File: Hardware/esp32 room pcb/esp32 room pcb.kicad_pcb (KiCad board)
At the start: 2 copper layers, 34.5 x 65.5 mm, 6 parts, among them Q1 AO3400A

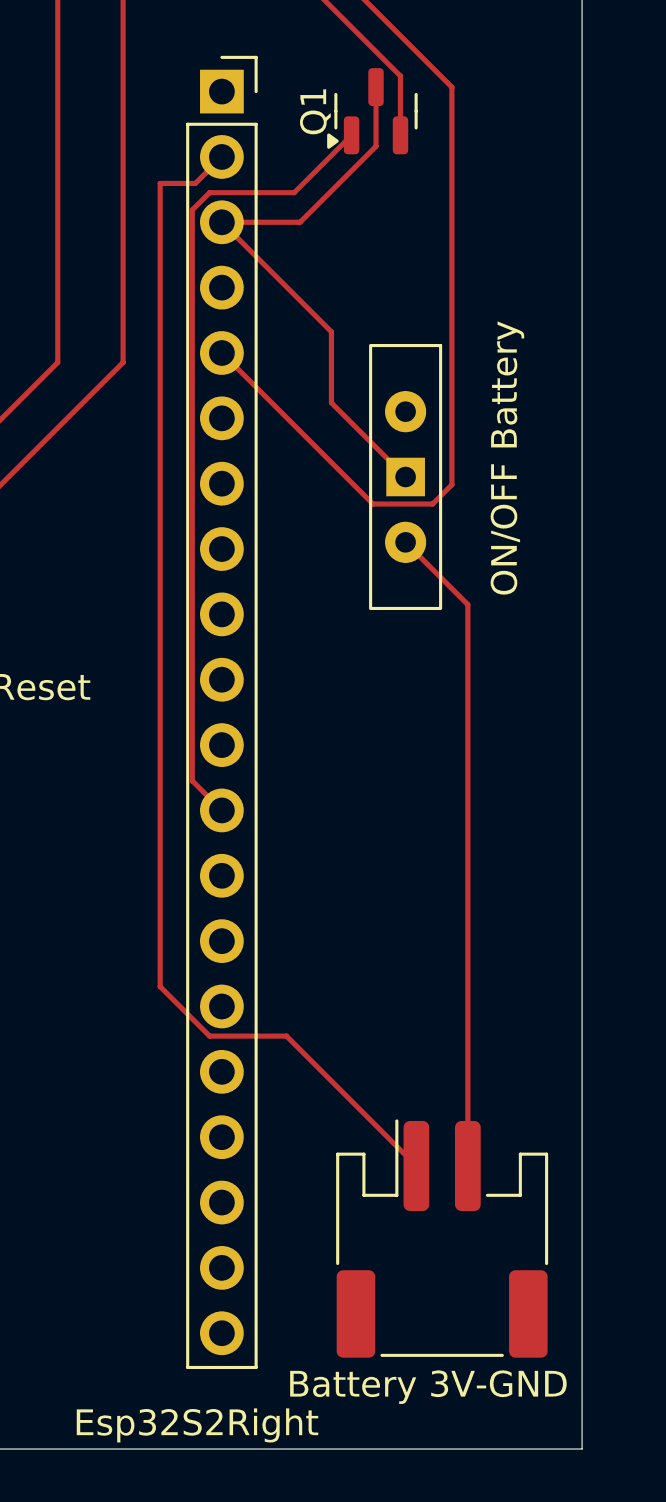
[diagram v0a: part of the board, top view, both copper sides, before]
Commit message: modification of foot print for battery connector
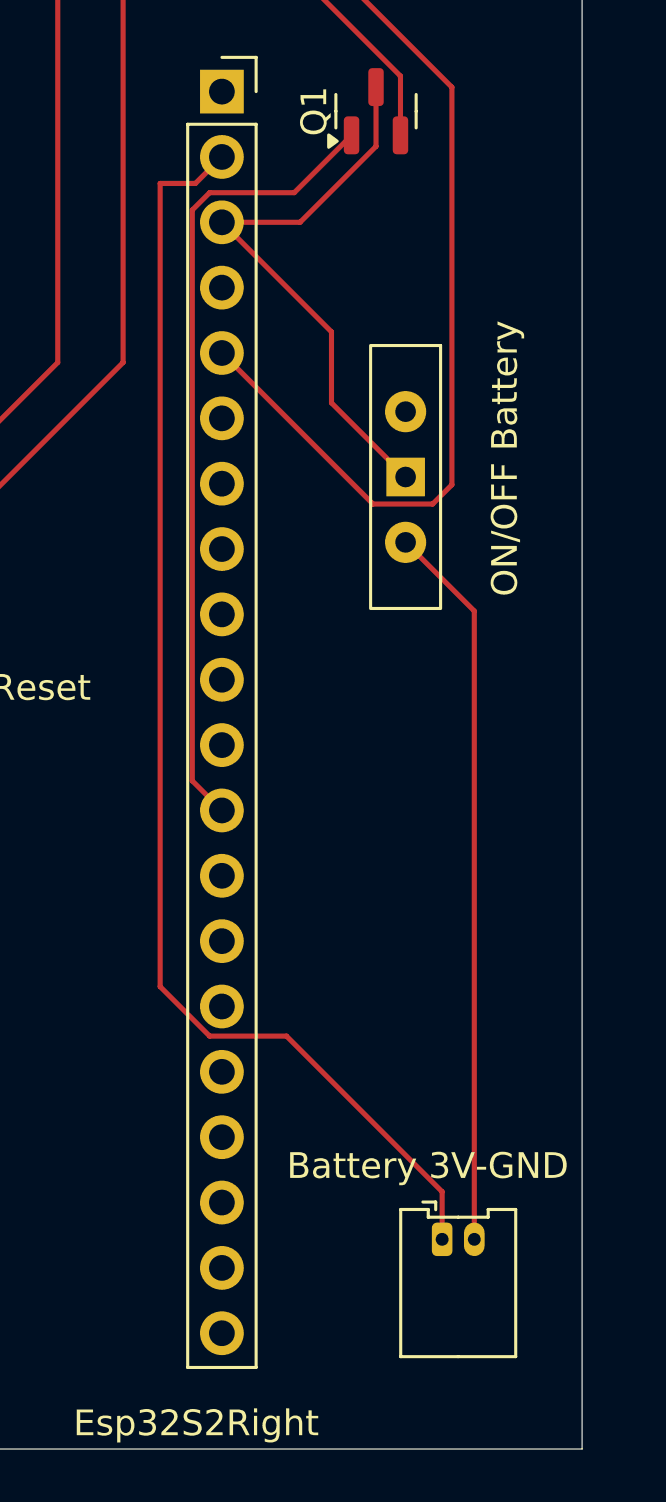
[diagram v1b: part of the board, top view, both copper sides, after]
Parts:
- Battery 3V-GND: footprint Connector_JST:JST_PH_S2B-PH-SM4-TB_1x02-1MP_P2.00mm_Horizontal -> Connector_Molex:Molex_PicoBlade_53048-0210_1x02_P1.25mm_Horizontal
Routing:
- net Vsys: track 46.9 -> 50.2 mm
- net Net-(J2-Pin_2): track 25.2 -> 28.2 mm

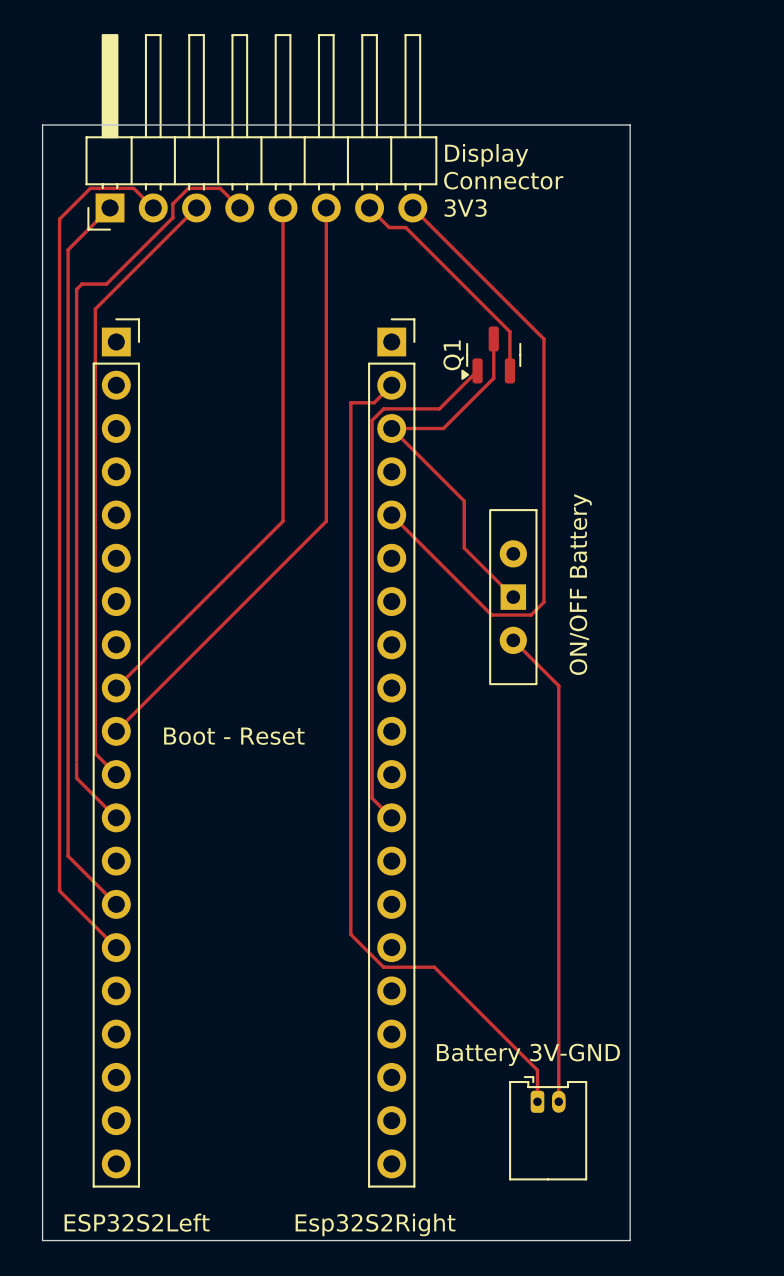
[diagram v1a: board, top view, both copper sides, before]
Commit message: modification of the switch to a cheaper on
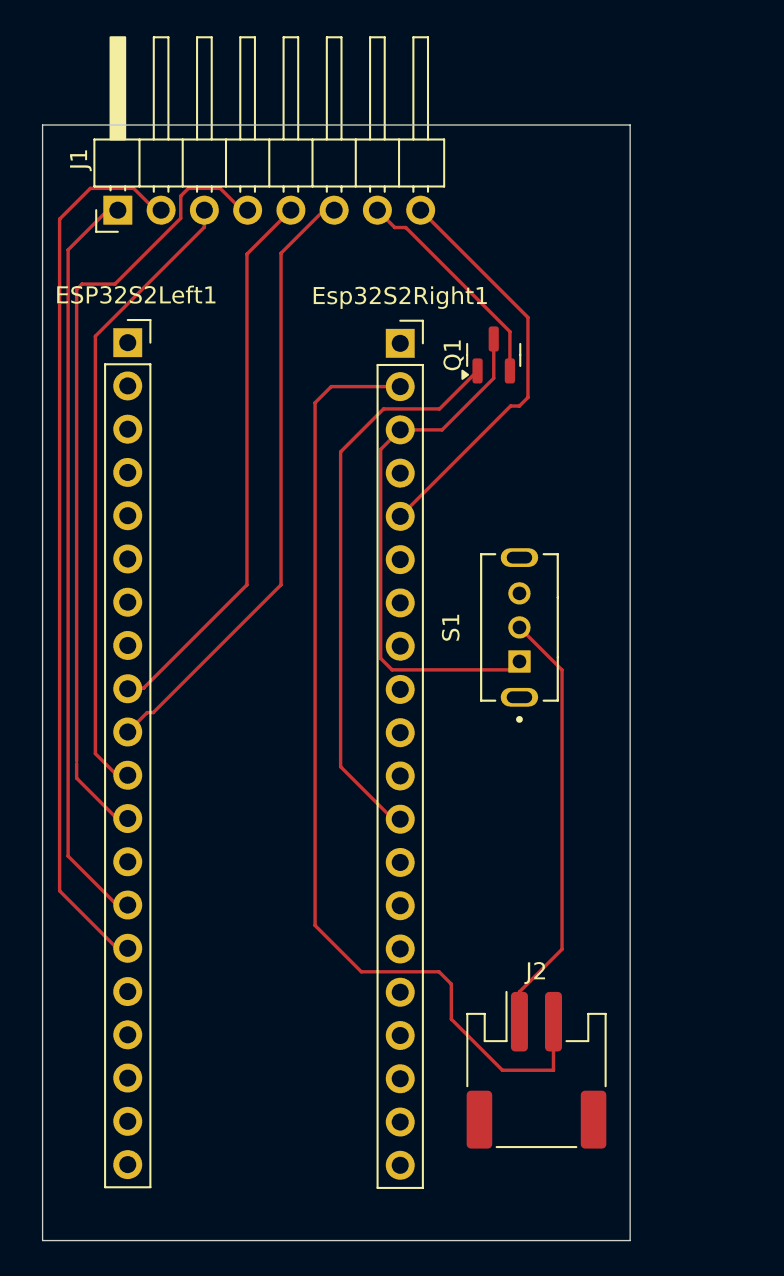
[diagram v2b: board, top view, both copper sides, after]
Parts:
- removed Battery 3V-GND: BATTERY connector, Connector_Molex:Molex_PicoBlade_53048-0210_1x02_P1.25mm_Horizontal
- removed Display Connector: DISPLAY connector, Connector_PinHeader_2.54mm:PinHeader_1x08_P2.54mm_Horizontal
- removed ESP32S2Left: Left pins, Connector_PinSocket_2.54mm:PinSocket_1x20_P2.54mm_Vertical
- removed Esp32S2Right: Right pins, Connector_PinSocket_2.54mm:PinSocket_1x20_P2.54mm_Vertical
- removed ON/OFF Battery: SW_Wuerth_450301014042, Button_Switch_THT:SW_Slide-03_Wuerth-WS-SLTV_10x2.5x6.4_P2.54mm
- added ESP32S2Left1: Left pins, Connector_PinSocket_2.54mm:PinSocket_1x20_P2.54mm_Vertical, F.Cu at (100.5, 76.8)
- added Esp32S2Right1: Right pins, Connector_PinSocket_2.54mm:PinSocket_1x20_P2.54mm_Vertical, F.Cu at (116.5, 76.8)
- added J1: DISPLAY connector, Connector_PinHeader_2.54mm:PinHeader_1x08_P2.54mm_Horizontal, F.Cu at (99.9, 69.0)
- added J2: BATTERY connector, Connector_JST:JST_PH_S2B-PH-SM4-TB_1x02-1MP_P2.00mm_Horizontal, F.Cu at (124.5, 119.5)
- added S1: SLW-864574-5A-RA-N-D, Library:SW_SLW-864574-5A-RA-N-D, F.Cu at (123.5, 93.5)
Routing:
- net Net-(J2-Pin_2): track 28.2 -> 0.00 mm
- net Net-(J2-Pin_1): track 0.00 -> 25.2 mm
- net 3V3: track 38.0 -> 24.9 mm
- net GND: track 22.4 -> 31.6 mm
- net Vsys: track 50.2 -> 57.7 mm
- net PWR: track 31.2 -> 33.3 mm
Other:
- board text removed: "3V3"
- board text removed: "Boot - Reset"

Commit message: corection et modification des bugs du à la basse tension (PCB + Arduino)
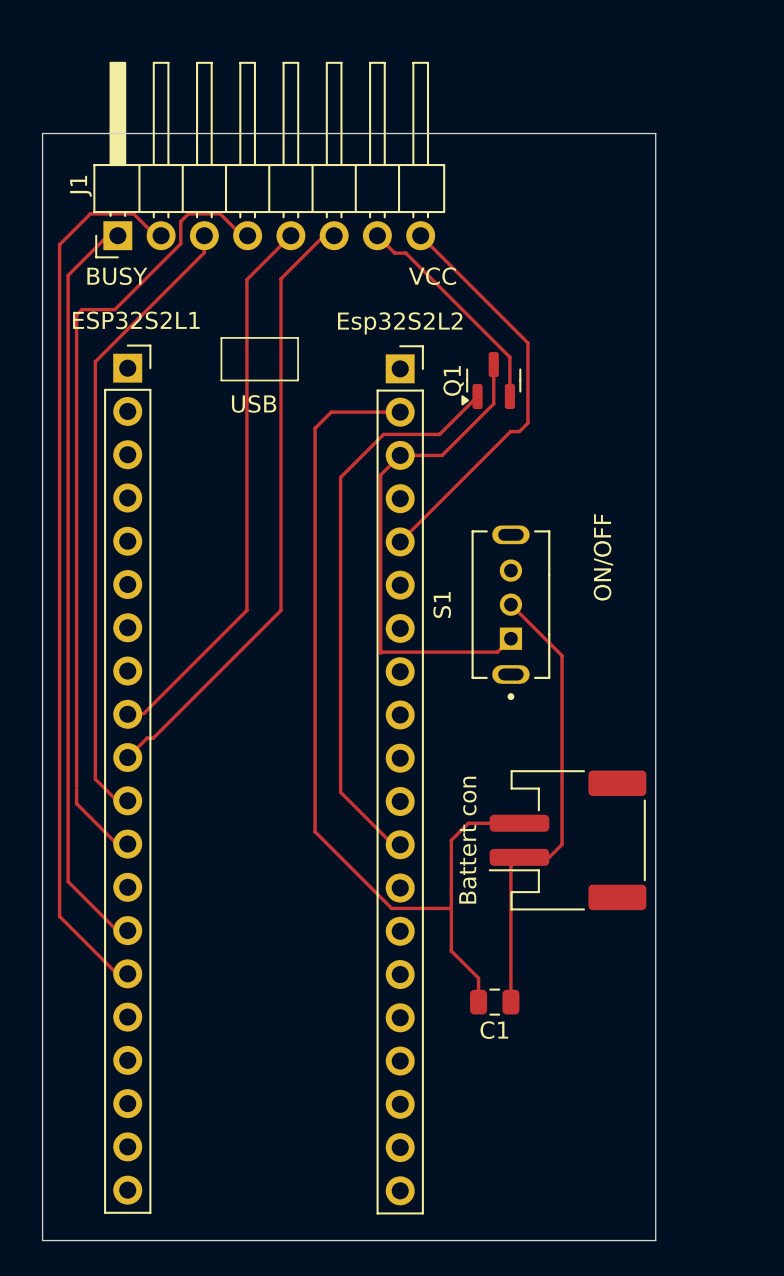
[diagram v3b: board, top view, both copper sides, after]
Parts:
- removed J2: BATTERY connector, Connector_JST:JST_PH_S2B-PH-SM4-TB_1x02-1MP_P2.00mm_Horizontal
- added Battert con: BATTERY connector, Connector_JST:JST_PH_S2B-PH-SM4-TB_1x02-1MP_P2.00mm_Horizontal, F.Cu at (126.3, 106.0)
- added C1: 10uF, Capacitor_SMD:C_0805_2012Metric, F.Cu at (122.0, 115.5)
- moved ESP32S2L1 1.50 mm to (100.5, 78.3)
- moved Esp32S2L2 1.50 mm to (116.5, 78.3)
- moved J1 1.50 mm to (99.9, 70.5)
- moved Q1 1.50 mm to (122.0, 79.0)
- moved S1 1.43 mm to (123.0, 92.2)
- renumbered ESP32S2Left1 to ESP32S2L1, Esp32S2Right1 to Esp32S2L2
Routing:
- net Vsys: track 57.7 -> 53.5 mm
- net Net-(J2-Pin_1): track 25.2 -> 28.6 mm
- net GND: track 31.6 -> 29.1 mm
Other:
- board size 34.5 x 65.5 mm -> 36 x 65 mm
- board text added: "BUSY"
- board text added: "ON/OFF"
- board text added: "USB"
- board text added: "VCC"

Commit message: ajout d'un booster 5V pcb
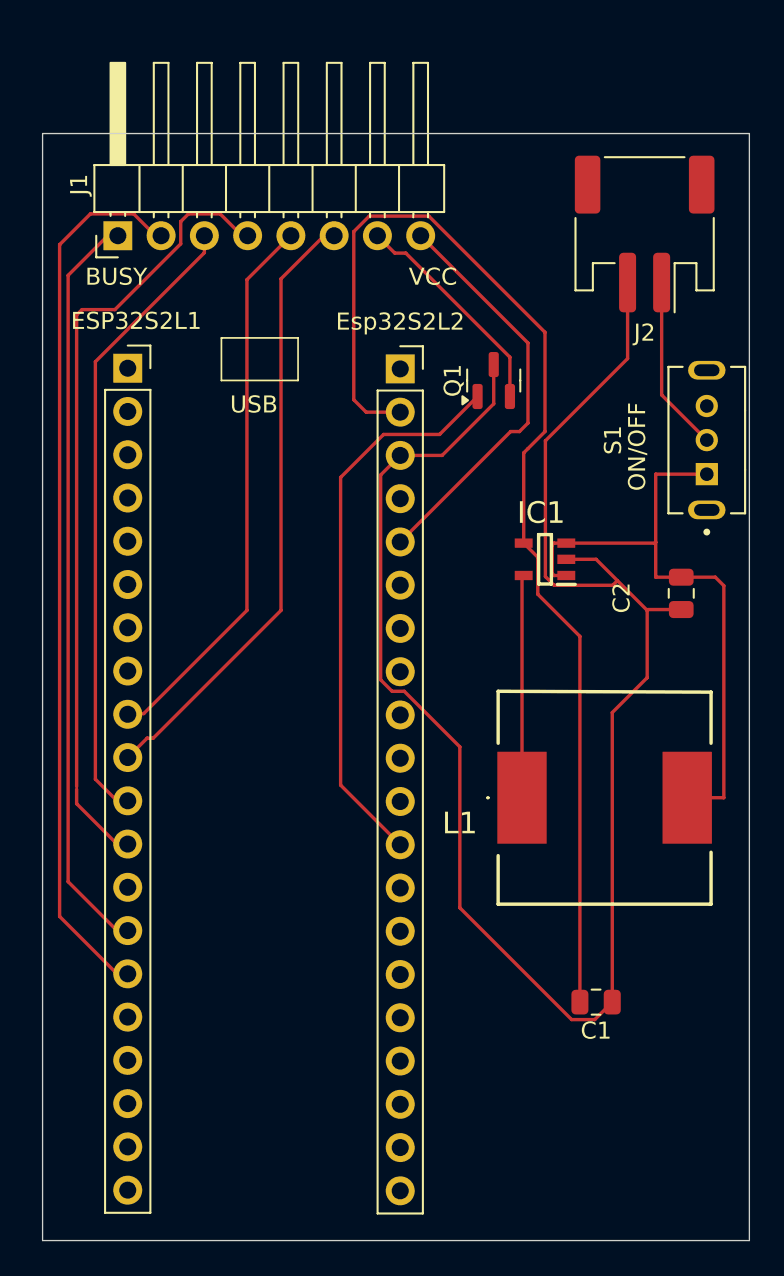
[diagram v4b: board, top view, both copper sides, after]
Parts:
- removed Battert con: BATTERY connector, Connector_JST:JST_PH_S2B-PH-SM4-TB_1x02-1MP_P2.00mm_Horizontal
- added C2: 10uF, Capacitor_SMD:C_0805_2012Metric, F.Cu at (133.0, 91.5)
- added IC1: MAX1724EZK50+T, Library:SOT95P275X110-5N, F.Cu at (125.0, 89.5)
- added J2: BATTERY connector, Connector_JST:JST_PH_S2B-PH-SM4-TB_1x02-1MP_P2.00mm_Horizontal, F.Cu at (130.8, 70.4)
- added L1: L, Library:SRR1260100M, F.Cu at (128.5, 103.5)
- moved S1 15.0 mm to (134.5, 82.5)
- moved C1 5.95 mm to (128.0, 115.5)
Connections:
- C1 pad 1: Net-(J2-Pin_1) -> GND
- S1 pad 1: GND -> Net-(IC1-BATT)
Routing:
- net GND: track 29.1 -> 106.2 mm
- net Net-(IC1-BATT): track 0.00 -> 36.6 mm
- net Net-(J2-Pin_1): track 28.6 -> 10.3 mm
- net Vsys: track 53.5 -> 68.5 mm
- net Net-(IC1-LX): track 0.00 -> 13.1 mm
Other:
- board size 36 x 65 mm -> 41.5 x 65 mm
